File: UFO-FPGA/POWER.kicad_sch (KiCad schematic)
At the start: 41 parts, among them J5 USB_B_Micro, Q1 2N7002

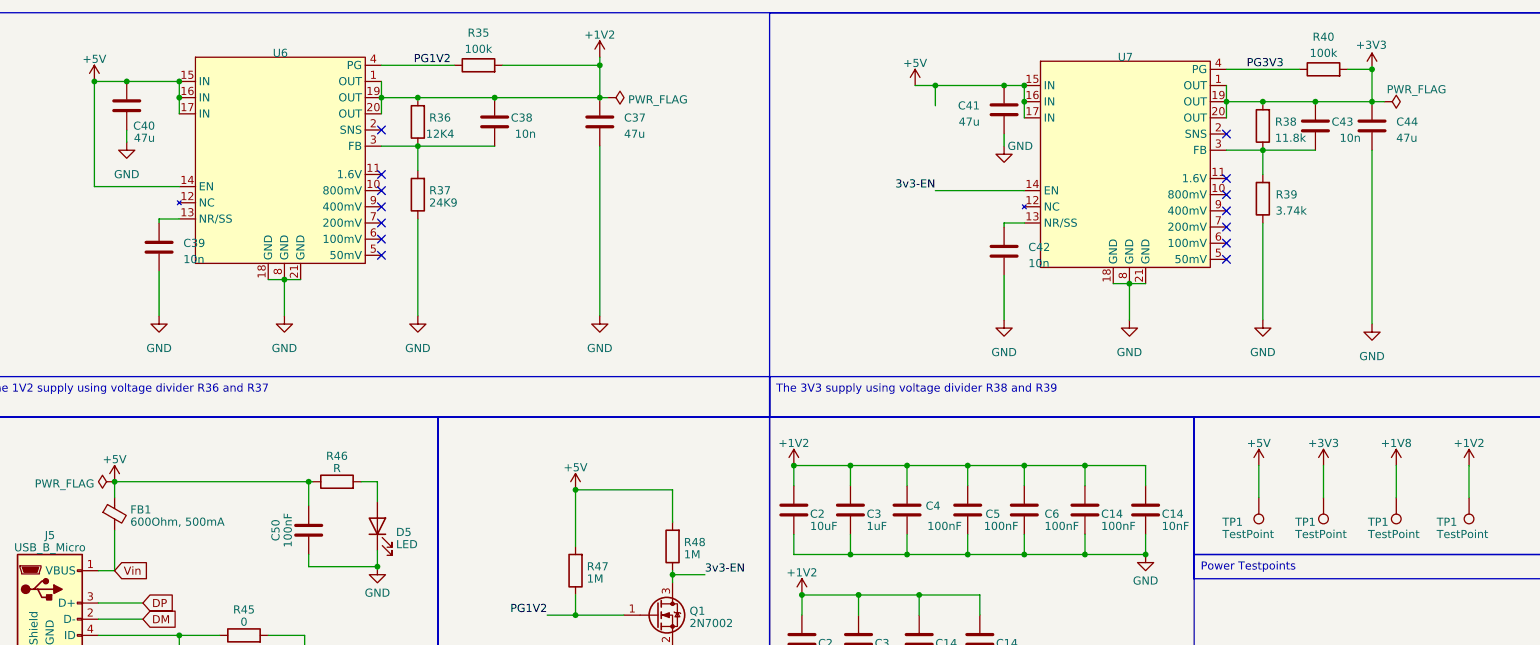
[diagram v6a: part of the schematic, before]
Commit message: PCB and footprint
Added foorprints and moved on pcb layout
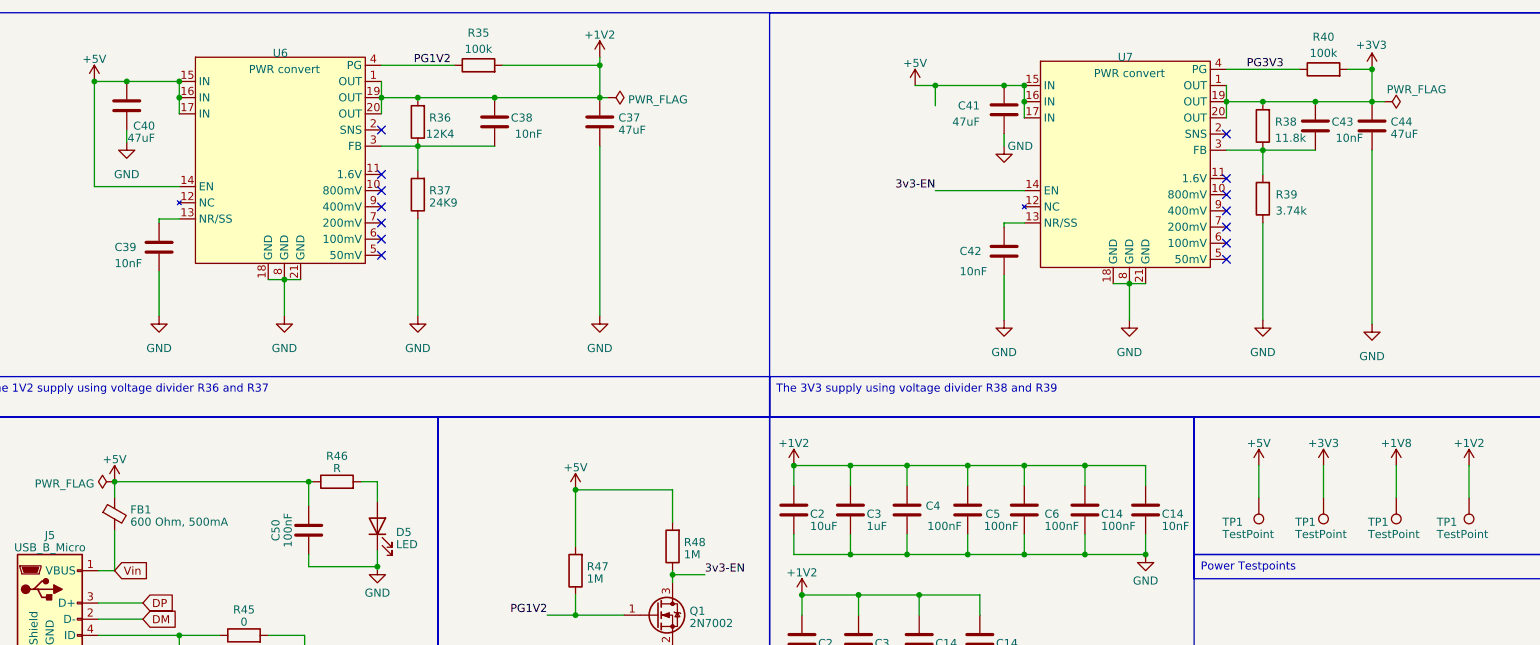
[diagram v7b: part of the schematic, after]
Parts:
- C37, C40, C41, C44: value 47u -> 47uF
- C38, C39, C42, C43: value 10n -> 10nF
- FB1: value 600Ohm, 500mA -> 600 Ohm, 500mA
- J5: footprint (none) -> Connector_USB:USB_Micro-AB_Molex_47590-0001
- U6, U7: value ~ -> PWR convert; footprint (none) -> UFO-Footpints:W-QFN3535-20
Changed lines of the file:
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@@
       (effects (font (size 1.27 1.27)) (justify left))
     )
-    (property "Value" "10n" (at 237.49 34.925 0)
+    (property "Value" "10nF" (at 236.855 34.925 0)
       (effects (font (size 1.27 1.27)) (justify left))
     )
@@
   )
   (symbol (lib_id "Device:C") (at 52.07 52.07 0) (unit 1)
-    (in_bom yes) (on_board yes) (dnp no) (fields_autoplaced)
-    (property "Reference" "C39" (at 55.88 51.435 0)
-      (effects (font (size 1.27 1.27)) (justify left))
-    )
-    (property "Value" "10n" (at 55.88 53.975 0)
+    (in_bom yes) (on_board yes) (dnp no)
+    (property "Reference" "C39" (at 45.085 52.07 0)
+      (effects (font (size 1.27 1.27)) (justify left))
+    )
+    (property "Value" "10nF" (at 45.085 54.61 0)
       (effects (font (size 1.27 1.27)) (justify left))
     )
@@
       (effects (font (size 1.27 1.27)))
     )
-    (property "Value" "~" (at 204.47 24.765 0)
-      (effects (font (size 1.27 1.27)))
-    )
-    (property "Footprint" "" (at 204.47 24.765 0)
+    (property "Value" "PWR convert" (at 204.47 24.765 0)
+      (effects (font (size 1.27 1.27)))
+    )
+    (property "Footprint" "UFO-Footpints:W-QFN3535-20" (at 204.47 24.765 0)
       (effects (font (size 1.27 1.27)) hide)
     )
@@
       (effects (font (size 1.27 1.27)) (justify left))
     )
-    (property "Value" "600Ohm, 500mA" (at 47.5488 95.2192 0)
+    (property "Value" "600 Ohm, 500mA" (at 47.5488 95.2192 0)
       (effects (font (size 1.27 1.27)) (justify left))
     )
@@
   (symbol (lib_id "Device:C") (at 121.285 32.385 0) (unit 1)
     (in_bom yes) (on_board yes) (dnp no) (fields_autoplaced)
-    (property "Reference" "C37" (at 125.095 31.75 0)
-      (effects (font (size 1.27 1.27)) (justify left))
-    )
-    (property "Value" "47u" (at 125.095 34.29 0)
+    (property "Reference" "C37" (at 124.206 31.7413 0)
+      (effects (font (size 1.27 1.27)) (justify left))
+    )
+    (property "Value" "47uF" (at 124.206 33.6623 0)
       (effects (font (size 1.27 1.27)) (justify left))
     )
@@
       (effects (font (size 1.27 1.27)))
     )
-    (property "Value" "~" (at 71.755 24.13 0)
-      (effects (font (size 1.27 1.27)))
-    )
-    (property "Footprint" "" (at 71.755 24.13 0)
+    (property "Value" "PWR convert" (at 71.755 24.13 0)
+      (effects (font (size 1.27 1.27)))
+    )
+    (property "Footprint" "UFO-Footpints:W-QFN3535-20" (at 71.755 24.13 0)
       (effects (font (size 1.27 1.27)) hide)
     )
@@
       (effects (font (size 1.27 1.27)) (justify left))
     )
-    (property "Value" "47u" (at 51.435 34.925 0)
+    (property "Value" "47uF" (at 51.435 34.925 0)
       (effects (font (size 1.27 1.27)) (justify left))
     )
@@
       (effects (font (size 1.27 1.27)))
     )
-    (property "Footprint" "" (at 38.735 109.22 0)
+    (property "Footprint" "Connector_USB:USB_Micro-AB_Molex_47590-0001" (at 38.735 109.22 0)
       (effects (font (size 1.27 1.27)) hide)
     )
@@
       (project "UFO-FPGA"
         (path "/b3168f6a-c732-41d3-aeeb-d97dd2f1bb65/abe08156-b909-4d2d-ad35-f723f4a728d5"
-          (reference "J1") (unit 1)
+          (reference "J5") (unit 1)
         )
       )
@@
       (effects (font (size 1.27 1.27)) (justify left))
     )
-    (property "Value" "10n" (at 107.95 34.29 0)
+    (property "Value" "10nF" (at 107.95 34.29 0)
       (effects (font (size 1.27 1.27)) (justify left))
     )
@@
   (symbol (lib_id "Device:C") (at 242.57 33.02 0) (unit 1)
     (in_bom yes) (on_board yes) (dnp no) (fields_autoplaced)
-    (property "Reference" "C44" (at 246.38 32.385 0)
-      (effects (font (size 1.27 1.27)) (justify left))
-    )
-    (property "Value" "47u" (at 246.38 34.925 0)
+    (property "Reference" "C44" (at 245.491 32.3763 0)
+      (effects (font (size 1.27 1.27)) (justify left))
+    )
+    (property "Value" "47uF" (at 245.491 34.2973 0)
       (effects (font (size 1.27 1.27)) (justify left))
     )
@@
       (effects (font (size 1.27 1.27)) (justify left))
     )
-    (property "Value" "47u" (at 180.975 32.385 0)
+    (property "Value" "47uF" (at 180.975 32.385 0)
       (effects (font (size 1.27 1.27)) (justify left))
     )
@@
   )
   (symbol (lib_id "Device:C") (at 184.785 52.705 0) (unit 1)
-    (in_bom yes) (on_board yes) (dnp no) (fields_autoplaced)
-    (property "Reference" "C42" (at 188.595 52.07 0)
-      (effects (font (size 1.27 1.27)) (justify left))
-    )
-    (property "Value" "10n" (at 188.595 54.61 0)
-      (effects (font (size 1.27 1.27)) (justify left))
-    )
+    (in_bom yes) (on_board yes) (dnp no)
+    (property "Reference" "C42" (at 177.8 52.705 0)
+      (effects (font (size 1.27 1.27)) (justify left))
+    )
+    (property "Value" "10nF" (at 177.8 55.88 0)
+      (effects (font (size 1.27 1.27)) (justify left))
+    )

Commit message: edge cuts
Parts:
- added R48: 1M, symbol Device:R
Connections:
- net +5V: now also R48.2; no longer U6.14 (EN)
- new net: R48.1, U6.14 (EN)
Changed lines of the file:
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@@
     (stroke (width 0) (type default))
   )
-  (wire (pts (xy 41.91 26.035) (xy 41.91 42.545))
+  (wire (pts (xy 41.91 26.035) (xy 41.91 31.75))
     (stroke (width 0) (type default))
   )
@@
   )
   (wire (pts (xy 161.925 106.68) (xy 171.45 106.68))
+    (stroke (width 0) (type default))
+  )
+  (wire (pts (xy 41.91 39.37) (xy 41.91 42.545))
     (stroke (width 0) (type default))
   )
@@
         )
       )
+    )
+  )
+  (symbol (lib_id "Device:R") (at 41.91 35.56 0) (mirror x) (unit 1)
+    (in_bom yes) (on_board yes) (dnp no)
+    (property "Reference" "R48" (at 40.132 34.9163 0)
+      (effects (font (size 1.27 1.27)) (justify right))
+    )
+    (property "Value" "1M" (at 40.132 36.8373 0)
+      (effects (font (size 1.27 1.27)) (justify right))
+    )
+    (property "Footprint" "" (at 40.132 35.56 90)
+      (effects (font (size 1.27 1.27)) hide)
+    )
+    (property "Datasheet" "~" (at 41.91 35.56 0)
+      (effects (font (size 1.27 1.27)) hide)
+    )
+    (pin "1")
+    (pin "2")
+    (instances
+      (project "POWER"
+        (path "/1a19c6f3-4fbd-4092-903c-8e5414c10419"
+          (reference "R48") (unit 1)
+        )
+      )
+      (project "UFO-FPGA"
+        (path "/b3168f6a-c732-41d3-aeeb-d97dd2f1bb65/abe08156-b909-4d2d-ad35-f723f4a728d5"
+          (reference "R55") (unit 1)
+        )
+      )
